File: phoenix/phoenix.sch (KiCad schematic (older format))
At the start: 1 part

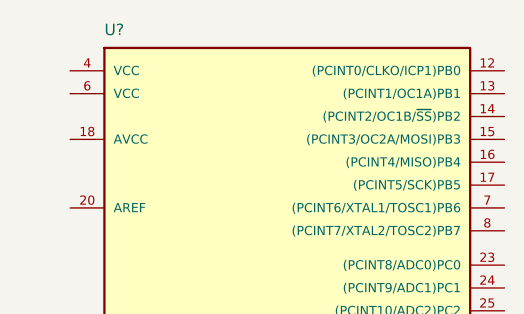
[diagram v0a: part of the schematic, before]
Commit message: added components
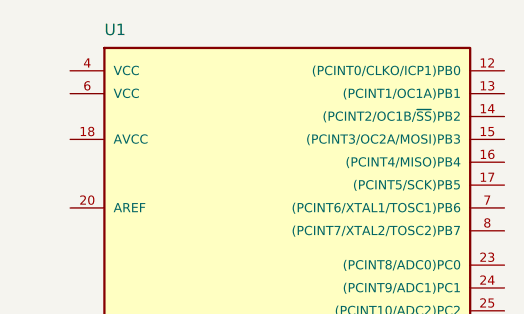
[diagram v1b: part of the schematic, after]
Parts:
- gave numbers to parts that had none: 1
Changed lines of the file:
@@
 LIBS:contrib
 LIBS:valves
+LIBS:phoenix-cache
 EELAYER 25 0
 EELAYER END
@@
 $EndDescr
 $Comp
-L ATMEGA328P-AU U?
+L ATMEGA328P-AU U1
 U 1 1 5A8B2ED4
 P 3000 2600
-F 0 "U?" H 2250 3850 50  0000 L BNN
+F 0 "U1" H 2250 3850 50  0000 L BNN
 F 1 "ATMEGA328P-AU" H 3400 1200 50  0000 L BNN
 F 2 "Housings_QFP:TQFP-32_7x7mm_Pitch0.8mm" H 3000 2600 50  0001 C CIN

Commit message: added more components to the library and also included all of formula's components to the library
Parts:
- added BT?: 3.7V Lipo, symbol Battery_Cell
- added C?: 12V Cap, symbol C
- added D?: D_Schottky, symbol D_Schottky
- added J?: Micro_SD_Card_Det, symbol Micro_SD_Card_Det
- added J?: Ultrafit_4, footprints:Ultrafit_4, symbol Ultrafit_4
- added Q? (x2): 2N2219, TO_SOT_Packages_THT:TO-39-3, symbol 2N2219
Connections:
- net labels added: 0V, 12V, VCC, sig+, sig-
- wire segments 0 -> 2
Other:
- moved on the sheet: U1
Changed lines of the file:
@@
 LIBS:contrib
 LIBS:valves
+LIBS:rocketry
 LIBS:phoenix-cache
 EELAYER 25 0
@@
 $EndDescr
 $Comp
+L C C?
+U 1 1 5ABA3966
+P 5100 1100
+F 0 "C?" V 4950 1050 50  0000 L CNN
+F 1 "12V Cap" V 5250 950 50  0000 L CNN
+F 2 "" H 5138 950 50  0001 C CNN
+F 3 "" H 5100 1100 50  0001 C CNN
+	1    5100 1100
+	0    1    1    0
+$EndComp
+$Comp
+L Battery_Cell BT?
+U 1 1 5ABA39D7
+P 1250 1100
+F 0 "BT?" V 1400 1100 50  0000 L CNN
+F 1 "3.7V Lipo" V 1050 950 50  0000 L CNN
+F 2 "" V 1250 1160 50  0001 C CNN
+F 3 "" V 1250 1160 50  0001 C CNN
+	1    1250 1100
+	0    -1   -1   0
+$EndComp
+$Comp
+L 2N2219 Q?
+U 1 1 5ABA3A12
+P 4750 1950
+F 0 "Q?" H 4950 2025 50  0000 L CNN
+F 1 "2N2219" H 4950 1950 50  0000 L CNN
+F 2 "TO_SOT_Packages_THT:TO-39-3" H 4950 1875 50  0001 L CIN
+F 3 "" H 4750 1950 50  0001 L CNN
+	1    4750 1950
+	1    0    0    -1
+$EndComp
+$Comp
+L 2N2219 Q?
+U 1 1 5ABA3A3B
+P 5550 1950
+F 0 "Q?" H 5750 2025 50  0000 L CNN
+F 1 "2N2219" H 5750 1950 50  0000 L CNN
+F 2 "TO_SOT_Packages_THT:TO-39-3" H 5750 1875 50  0001 L CIN
+F 3 "" H 5550 1950 50  0001 L CNN
+	1    5550 1950
+	1    0    0    -1
+$EndComp
+$Comp
+L Micro_SD_Card_Det J?
+U 1 1 5ABA3E17
+P 6350 4700
+F 0 "J?" H 5700 5400 50  0000 C CNN
+F 1 "Micro_SD_Card_Det" H 7000 5400 50  0000 R CNN
+F 2 "" H 8400 5400 50  0001 C CNN
+F 3 "" H 6350 4800 50  0001 C CNN
+	1    6350 4700
+	1    0    0    -1
+$EndComp
+$Comp
 L ATMEGA328P-AU U1
 U 1 1 5A8B2ED4
-P 3000 2600
-F 0 "U1" H 2250 3850 50  0000 L BNN
-F 1 "ATMEGA328P-AU" H 3400 1200 50  0000 L BNN
-F 2 "Housings_QFP:TQFP-32_7x7mm_Pitch0.8mm" H 3000 2600 50  0001 C CIN
-F 3 "" H 3000 2600 50  0001 C CNN
-	1    3000 2600
+P 2700 3850
+F 0 "U1" H 1950 5100 50  0000 L BNN
+F 1 "ATMEGA328P-AU" H 3100 2450 50  0000 L BNN
+F 2 "Housings_QFP:TQFP-32_7x7mm_Pitch0.8mm" H 2700 3850 50  0001 C CIN
+F 3 "" H 2700 3850 50  0001 C CNN
+	1    2700 3850
 	1    0    0    -1
 $EndComp
-Text Label 2100 3600 2    60   ~ 0
+Text Label 1050 1100 2    60   ~ 0
+VCC
+Text Label 1350 1100 0    60   ~ 0
 GND
-Text Label 2100 3700 2    60   ~ 0
+Text Label 1800 2750 2    60   ~ 0
+VCC
+Text Label 1800 2850 2    60   ~ 0
+VCC
+Text Label 1800 4850 2    60   ~ 0
 GND
-Text Label 2100 3800 2    60   ~ 0
+Text Label 1800 4950 2    60   ~ 0
 GND
+Text Label 1800 5050 2    60   ~ 0
+GND
+Text Label 4450 1100 2    60   ~ 0
+12V
+Text Label 5250 1100 0    60   ~ 0
+0V
+$Comp
+L D_Schottky D?
+U 1 1 5ABA4F03
+P 4600 1100
+F 0 "D?" H 4600 1200 50  0000 C CNN
+F 1 "D_Schottky" H 4600 1000 50  0000 C CNN
+F 2 "" H 4600 1100 50  0001 C CNN
+F 3 "" H 4600 1100 50  0001 C CNN
+	1    4600 1100
+	-1   0    0    1
+$EndComp
+Text Label 5650 1750 1    60   ~ 0
+12V
+Wire Wire Line
+	4750 1100 4950 1100
+Wire Wire Line
+	4850 1100 4850 1750
+Connection ~ 4850 1100
+$Comp
+L Ultrafit_4 J?
+U 1 1 5ABA5620
+P 1150 1700
+F 0 "J?" H 1150 2000 60  0000 C CNN
+F 1 "Ultrafit_4" H 1150 1500 60  0000 C CNN
+F 2 "footprints:Ultrafit_4" H 1050 1950 60  0001 C CNN
+F 3 "http://www.literature.molex.com/SQLImages/kelmscott/Molex/PDF_Images/987651-1008.pdf" H 1150 2050 60  0001 C CNN
+F 4 "Digi-Key" H 1150 1700 60  0001 C CNN "MFN"
+F 5 "Value" H 1150 1700 60  0001 C CNN "Package"
+F 6 "WM11574-ND" H 1150 1700 60  0001 C CNN "MPN"
+F 7 "WM11564-ND" H 1550 2450 60  0001 C CNN "MPN2"
+F 8 "https://www.digikey.com/products/en?keywords=WM11574-ND" H 1650 2550 60  0001 C CNN "PurchasingLink"
+F 9 "https://www.digikey.com/product-detail/en/molex-llc/1722561004/WM11564-ND/5291228" H 1750 2650 60  0001 C CNN "PurchasingLink2"
+	1    1150 1700
+	1    0    0    -1
+$EndComp
+Text Label 1500 1500 0    60   ~ 0
+12V
+Text Label 1500 1600 0    60   ~ 0
+0V
+Text Label 1500 1700 0    60   ~ 0
+sig+
+Text Label 1500 1800 0    60   ~ 0
+sig-
 $EndSCHEMATC

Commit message: Updated schematic
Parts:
- added C?: C_100pF, footprints:C_0805_OEM, symbol C_100pF
- added P?: CONN_02X03, footprints:Pin_Header_Straight_2x03, symbol CONN_02X03
- added R?: R_100, footprints:R_0805_OEM, symbol R_100
- added R?: R_10k, footprints:R_0805_OEM, symbol R_10k
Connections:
- net labels added: +3.3V, +BATT, 3.3V, MISO, MOSI, RESET, SCK, Spi_config
- wire segments 2 -> 19
- no-connect marks 0 -> 5

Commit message: Updated schematic
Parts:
- removed J?: Ultrafit_4, footprints:Ultrafit_4, symbol Ultrafit_4
- removed Q?: 2N2219, TO_SOT_Packages_THT:TO-39-3, symbol 2N2219
- added D? (x3): LED_0805, footprints:LED_0805_OEM, symbol LED_0805
- added J?: Ultrafit_2, footprints:Ultrafit_2, symbol Ultrafit_2
- added R? (x3): R_200, footprints:R_0805_OEM, symbol R_200
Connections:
- net labels added: PLED1, PLED2, PLED3, Sol+, Sol-
- net labels removed: sig+, sig-
- wire segments 19 -> 22
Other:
- note added: "Deployment (unfinished)"
- note added: "Micro SD-Card Reader"
- note added: "Programming LEDs"
- moved on the sheet: BT?, C?, D?, J?, P?, Q?, R?, U1

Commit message: added components to board
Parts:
- removed C?: 12V Cap, symbol C
- removed D?: D_Schottky, symbol D_Schottky
- removed Q?: 2N2219, TO_SOT_Packages_THT:TO-39-3, symbol 2N2219
- added C? (x2): C_0.1uF, footprints:C_0805_OEM, symbol C_0.1uF
- added C?: C_10uF, footprints:C_0805_OEM, symbol C_10uF
- added R?: R_10k, footprints:R_0805_OEM, symbol R_10k
- added U?: MMA8451QT, footprints:MMA8451QT, symbol MMA8451QT
- added U?: L6932D1.2, footprints:L6932D1.2TR, symbol L6932D1.2
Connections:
- net +3V3: now also C?.1, R?.2
- net GND: now also C?.2, C?.2, U?.10 (GND), U?.12 (GND), U?.5 (GND)
- net SDA: now reaches U1.27 ((PCINT12/SDA/ADC4)PC4)
- net SDA: now also U?.6 (SDA)
- net SCL: now reaches U1.28 ((PCINT13/SCL/ADC5)PC5)
- net SCL: now also U?.4 (SCL)
- new net: U?.1 (VDDIO), U?.14 (VDD)
- new net: R?.1, U?.7 (SA0)
- new net 3V7: C?.1
- new net BYP: C?.1, U?.2 (BYP)
- new net INT1: U?.11 (INT1)
- new net INT2: U?.9 (INT2)
- new net VIN: C?.2, U?.1 (EN), U?.2 (IN)
- no-connect marks 5 -> 10
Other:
- note removed: "Deployment (unfinished)"
- moved on the sheet: BT?, C?, D?, J?, P?, R?, U1

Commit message: added more parts
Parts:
- added C?: C_10uF, footprints:C_0805_OEM, symbol C_10uF
- added R?: 5K, symbol 5K
- added R?: 9K, symbol 5K
- added R?: R_10k, footprints:R_0805_OEM, symbol R_10k
- added ROCKET_IGNITER: R_200, footprints:R_0805_OEM, symbol R_200
- added U?: SI4838DY, symbol SI4838DY
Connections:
- net +3V3: now also U?.4 (OUT), R?.1, ROCKET_IGNITER.1
- net GND: now also U?.5 (GND), U?.6 (GND), U?.7 (GND), U?.8 (GND), C?.2, R?.2, R?.2, U?.1 (S), U?.2 (S), U?.3 (S)
- net SEPERATE: now reaches U1.11 ((PCINT23/AIN1)PD7)
- net SEPERATE: now also R?.1, U?.4 (G)
- net at U?.3 (AGJ): now also R?.1, R?.2
- new net: ROCKET_IGNITER.2, U?.5 (D), U?.6 (D), U?.7 (D), U?.8 (D)
- new net VOUT: C?.1
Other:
- moved on the sheet: C?

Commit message: Added external oscillator
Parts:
- added C? (x2): C_30pF, footprints:C_0805_OEM, symbol C_30pF
- added Y?: Crystal_SMD, footprints:Crystal_SMD_FA238, symbol Crystal_SMD
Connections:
- net GND: now also C?.2, C?.2, Y?.2, Y?.4
- new net PB6: C?.1, Y?.1
- new net PB7: C?.1, Y?.3
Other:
- note added: "Accelerometer"
- note added: "Linear Regulator\n"
- note added: "N-Channel Transistor\n"
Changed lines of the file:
@@
 Text Label 7600 2100 0    60   ~ 0
 VCC
+Text Notes 10650 4750 0    60   ~ 0
+Accelerometer
+Text Notes 11400 1600 0    60   ~ 0
+Linear Regulator\n
+Text Notes 5700 1750 0    60   ~ 0
+N-Channel Transistor\n
+$Comp
+L Crystal_SMD Y?
+U 1 1 5ACEF03D
+P 21650 2000
+F 0 "Y?" H 21700 2175 50  0000 L CNN
+F 1 "Crystal_SMD" H 21300 2300 50  0000 L CNN
+F 2 "footprints:Crystal_SMD_FA238" H 21600 2075 50  0001 C CNN
+F 3 "https://support.epson.biz/td/api/doc_check.php?dl=brief_FA-238V_en.pdf" H 21700 2175 50  0001 C CNN
+F 4 "Digi-Key" H 21650 2000 60  0001 C CNN "MFN"
+F 5 "SER3686CT-ND" H 21650 2000 60  0001 C CNN "MPN"
+F 6 "Value" H 21650 2000 60  0001 C CNN "Package"
+F 7 "https://www.digikey.com/products/en?keywords=SER3686CT-ND" H 22100 2575 60  0001 C CNN "PurchasingLink"
+	1    21650 2000
+	1    0    0    -1
+$EndComp
+Text Label 21950 1750 0    60   ~ 0
+GND
+Text Label 21650 2400 0    60   ~ 0
+GND
+$Comp
+L C_30pF C?
+U 1 1 5ACF00B7
+P 21400 2150
+F 0 "C?" H 21425 2250 50  0000 L CNN
+F 1 "C_30pF" H 21425 2050 50  0000 L CNN
+F 2 "footprints:C_0805_OEM" H 21438 2000 50  0001 C CNN
+F 3 "https://media.digikey.com/pdf/Data%20Sheets/Samsung%20PDFs/CL_Series_MLCC_ds.pdf" H 21425 2250 50  0001 C CNN
+F 4 "1276-1130-1-ND" H 21400 2150 60  0001 C CNN "MPN"
+F 5 "Digi-Key" H 21400 2150 60  0001 C CNN "MFN"
+F 6 "Value" H 21400 2150 60  0001 C CNN "Package"
+F 7 "https://www.digikey.com/product-detail/en/samsung-electro-mechanics-america-inc/CL21C300JBANNNC/1276-1130-1-ND/3889216" H 21825 2650 60  0001 C CNN "PurchasingLink"
+	1    21400 2150
+	1    0    0    -1
+$EndComp
+$Comp
+L C_30pF C?
+U 1 1 5ACF0160
+P 21900 2150
+F 0 "C?" H 21925 2250 50  0000 L CNN
+F 1 "C_30pF" H 21925 2050 50  0000 L CNN
+F 2 "footprints:C_0805_OEM" H 21938 2000 50  0001 C CNN
+F 3 "https://media.digikey.com/pdf/Data%20Sheets/Samsung%20PDFs/CL_Series_MLCC_ds.pdf" H 21925 2250 50  0001 C CNN
+F 4 "1276-1130-1-ND" H 21900 2150 60  0001 C CNN "MPN"
+F 5 "Digi-Key" H 21900 2150 60  0001 C CNN "MFN"
+F 6 "Value" H 21900 2150 60  0001 C CNN "Package"
+F 7 "https://www.digikey.com/product-detail/en/samsung-electro-mechanics-america-inc/CL21C300JBANNNC/1276-1130-1-ND/3889216" H 22325 2650 60  0001 C CNN "PurchasingLink"
+	1    21900 2150
+	1    0    0    -1
+$EndComp
+Wire Wire Line
+	21750 2000 22050 2000
+Connection ~ 21400 2000
+Wire Wire Line
+	21300 2000 21550 2000
+Text Label 21300 2000 2    60   ~ 0
+PB6
+Connection ~ 21900 2000
+Text Label 22050 2000 0    60   ~ 0
+PB7
+Wire Wire Line
+	21650 1850 21650 1750
+Wire Wire Line
+	21650 1750 21950 1750
+Wire Wire Line
+	21650 2150 21650 2400
+Wire Wire Line
+	21400 2300 21900 2300
+Connection ~ 21650 2300
 $EndSCHEMATC

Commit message: Edited schematic and added footpring
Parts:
- removed ROCKET_IGNITER: R_200, footprints:R_0805_OEM, symbol R_200
- gave numbers to parts that had none: 27
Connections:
- net 3.3V is gone; now on net +3V3: J2.4 (VDD)
- net 3V7 is gone; now on net VIN: C4.1
- net Sol+ is gone; now on net +3V3: J1.1
- net Sol- is gone; now on an unnamed net: J1.2
- net VOUT is gone; now on net +3V3: C3.1
- net +3V3: no longer BT1.1 (+)
- net GND: now also C4.2
- net INT1: now also U1.32 ((PCINT18/INT0)PD2)
- net INT2: now also U1.1 ((PCINT19/OC2B/INT1)PD3)
- net PB6: now also U1.7 ((PCINT6/XTAL1/TOSC1)PB6)
- net PB7: now also U1.8 ((PCINT7/XTAL2/TOSC2)PB7)
- net VIN: now also BT1.1 (+); no longer C4.2
- no-connect marks 10 -> 21
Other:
- moved on the sheet: C1, C2, J1
